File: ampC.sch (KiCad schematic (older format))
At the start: 9 parts, among them U3 MCP6004, U7 Mux

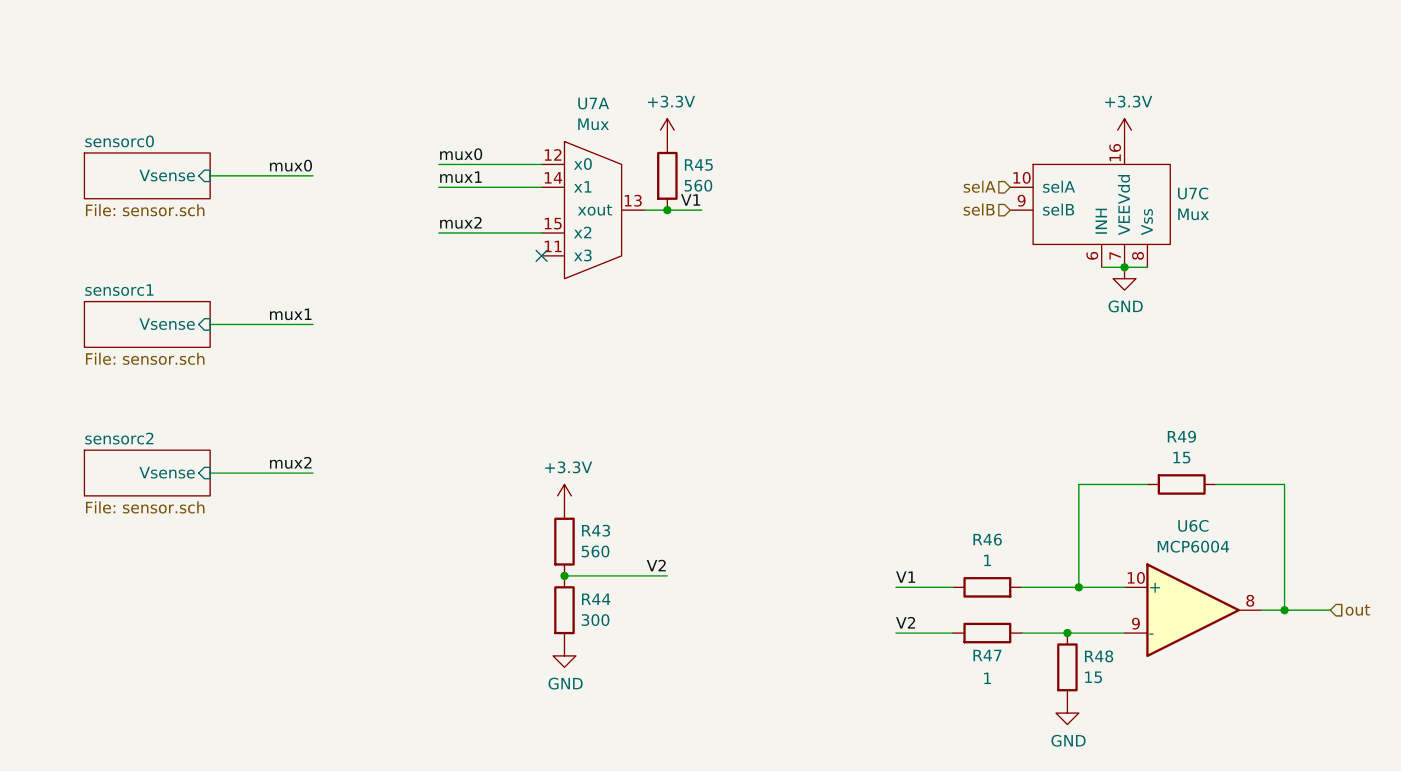
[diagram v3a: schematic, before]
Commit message: fixed drc errors
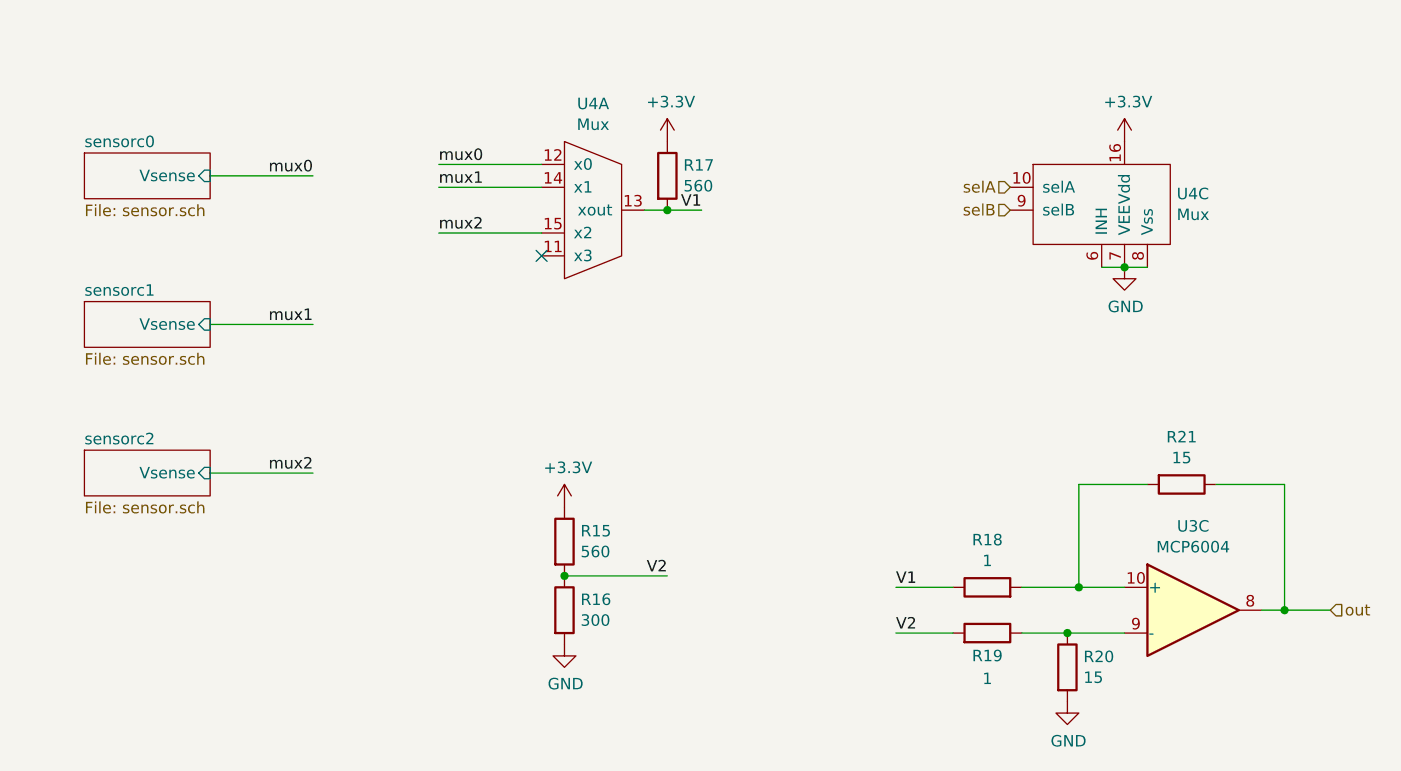
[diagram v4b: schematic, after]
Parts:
- U3: footprint Package_DIP:DIP-14_W7.62mm -> Package_SO:SOIC-16_3.9x9.9mm_P1.27mm
- U7: footprint Package_DIP:DIP-16_W7.62mm -> Package_SO:SOIC-16_3.9x9.9mm_P1.27mm
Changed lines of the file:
@@
 AR Path="/6019C043/60198F28" Ref="R20"  Part="1"
 AR Path="/601B4C16/60198F28" Ref="R48"  Part="1"
-F 0 "R48" H 5520 4096 50  0000 L CNN
+F 0 "R20" H 5520 4096 50  0000 L CNN
 F 1 "15" H 5520 4005 50  0000 L CNN
 F 2 "Resistor_THT:R_Axial_DIN0204_L3.6mm_D1.6mm_P5.08mm_Horizontal" V 5380 4050 50  0001 C CNN
@@
 AR Path="/6019C043/6019D567" Ref="R21"  Part="1"
 AR Path="/601B4C16/6019D567" Ref="R49"  Part="1"
-F 0 "R49" V 5743 3250 50  0000 C CNN
+F 0 "R21" V 5743 3250 50  0000 C CNN
 F 1 "15" V 5834 3250 50  0000 C CNN
 F 2 "Resistor_THT:R_Axial_DIN0204_L3.6mm_D1.6mm_P5.08mm_Horizontal" V 5880 3250 50  0001 C CNN
@@
 AR Path="/6019C043/6019D55D" Ref="R18"  Part="1"
 AR Path="/601B4C16/6019D55D" Ref="R46"  Part="1"
-F 0 "R46" V 5307 3700 50  0000 C CNN
+F 0 "R18" V 5307 3700 50  0000 C CNN
 F 1 "1" V 5216 3700 50  0000 C CNN
 F 2 "Resistor_THT:R_Axial_DIN0204_L3.6mm_D1.6mm_P5.08mm_Horizontal" V 5030 3700 50  0001 C CNN
@@
 AR Path="/6019C043/60198F34" Ref="R19"  Part="1"
 AR Path="/601B4C16/60198F34" Ref="R47"  Part="1"
-F 0 "R47" V 5000 3900 50  0000 C CNN
+F 0 "R19" V 5000 3900 50  0000 C CNN
 F 1 "1" V 4900 3900 50  0000 C CNN
 F 2 "Resistor_THT:R_Axial_DIN0204_L3.6mm_D1.6mm_P5.08mm_Horizontal" V 5030 3900 50  0001 C CNN
@@
 AR Path="/6019C043/6017E433" Ref="R15"  Part="1"
 AR Path="/601B4C16/6017E433" Ref="R43"  Part="1"
-F 0 "R43" H 3320 3546 50  0000 L CNN
+F 0 "R15" H 3320 3546 50  0000 L CNN
 F 1 "560" H 3320 3455 50  0000 L CNN
 F 2 "Resistor_THT:R_Axial_DIN0204_L3.6mm_D1.6mm_P5.08mm_Horizontal" V 3180 3500 50  0001 C CNN
@@
 AR Path="/6019C043/6017E434" Ref="R16"  Part="1"
 AR Path="/601B4C16/6017E434" Ref="R44"  Part="1"
-F 0 "R44" H 3320 3846 50  0000 L CNN
+F 0 "R16" H 3320 3846 50  0000 L CNN
 F 1 "300" H 3320 3755 50  0000 L CNN
 F 2 "Resistor_THT:R_Axial_DIN0204_L3.6mm_D1.6mm_P5.08mm_Horizontal" V 3180 3800 50  0001 C CNN
@@
 AR Path="/601B4C16/601763C1" Ref="U7"  Part="1"
 AR Path="/6019C043/601763C1" Ref="U4"  Part="1"
-F 0 "U7" H 3375 2515 50  0000 C CNN
+F 0 "U4" H 3375 2515 50  0000 C CNN
 F 1 "Mux" H 3375 2424 50  0000 C CNN
-F 2 "Package_DIP:DIP-16_W7.62mm" H 3350 2050 50  0001 C CNN
+F 2 "Package_SO:SOIC-16_3.9x9.9mm_P1.27mm" H 3350 2050 50  0001 C CNN
 F 3 "" H 3350 2050 50  0001 C CNN
 	1    3350 2050
@@
 AR Path="/601B4C16/60176BAF" Ref="U7"  Part="3"
 AR Path="/6019C043/60176BAF" Ref="U4"  Part="3"
-F 0 "U7" H 5928 2221 50  0000 L CNN
+F 0 "U4" H 5928 2221 50  0000 L CNN
 F 1 "Mux" H 5928 2130 50  0000 L CNN
-F 2 "Package_DIP:DIP-16_W7.62mm" H 5700 2100 50  0001 C CNN
+F 2 "Package_SO:SOIC-16_3.9x9.9mm_P1.27mm" H 5700 2100 50  0001 C CNN
 F 3 "" H 5700 2100 50  0001 C CNN
 	3    5700 2100
@@
 AR Path="/6019C043/6018DE62" Ref="U3"  Part="3"
 AR Path="/601B4C16/6018DE62" Ref="U6"  Part="3"
-F 0 "U6" H 6000 4167 50  0000 C CNN
+F 0 "U3" H 6000 4167 50  0000 C CNN
 F 1 "MCP6004" H 6000 4076 50  0000 C CNN
-F 2 "Package_DIP:DIP-14_W7.62mm" H 5950 3900 50  0001 C CNN
+F 2 "Package_SO:SOIC-16_3.9x9.9mm_P1.27mm" H 5950 3900 50  0001 C CNN
 F 3 "http://ww1.microchip.com/downloads/en/DeviceDoc/21733j.pdf" H 6050 4000 50  0001 C CNN
 	3    6000 3800
@@
 AR Path="/6019C043/60205F03" Ref="R17"  Part="1"
 AR Path="/601B4C16/60205F03" Ref="R45"  Part="1"
-F 0 "R45" H 3770 1946 50  0000 L CNN
+F 0 "R17" H 3770 1946 50  0000 L CNN
 F 1 "560" H 3770 1855 50  0000 L CNN
 F 2 "Resistor_THT:R_Axial_DIN0204_L3.6mm_D1.6mm_P5.08mm_Horizontal" V 3630 1900 50  0001 C CNN

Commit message: changed solder pads to be two separate footprints
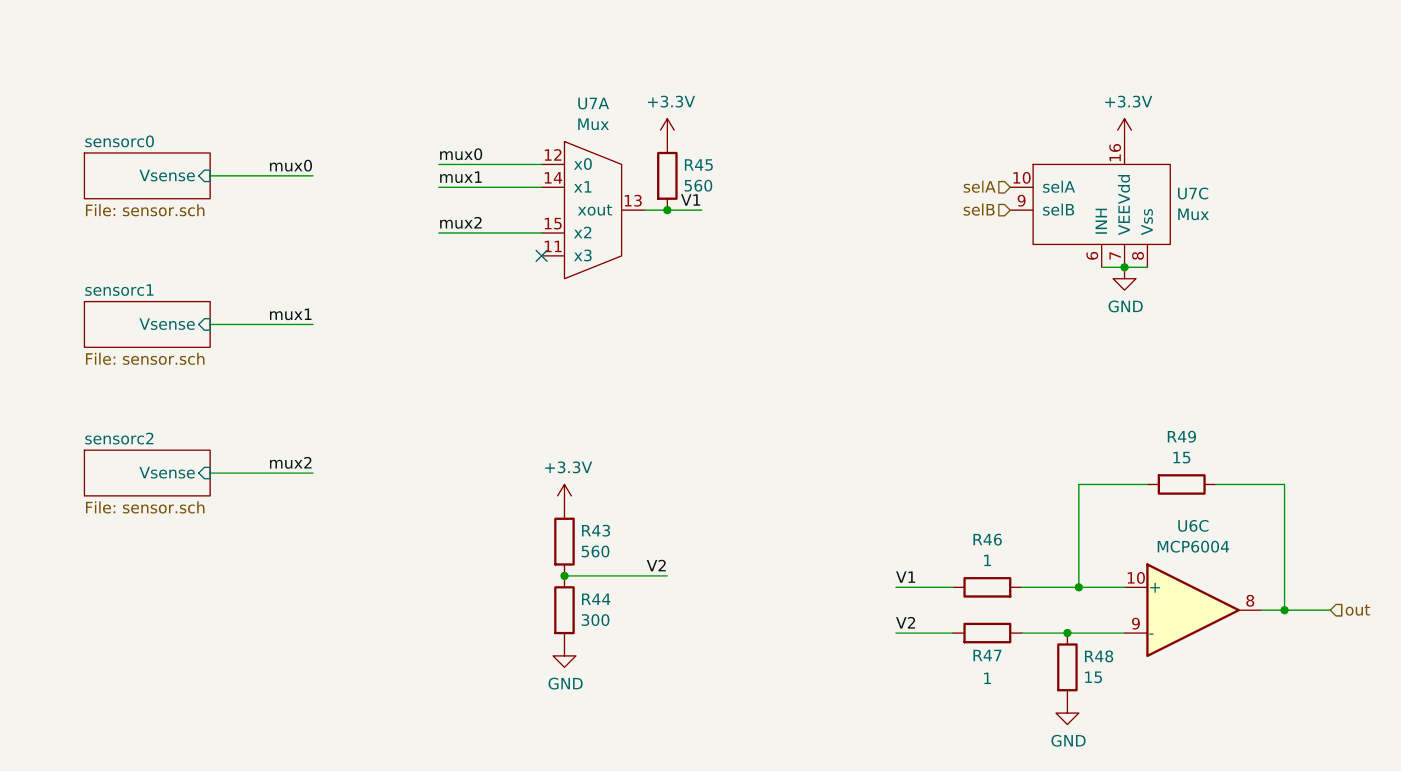
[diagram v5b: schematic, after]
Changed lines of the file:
@@
 AR Path="/6019C043/60198F28" Ref="R20"  Part="1"
 AR Path="/601B4C16/60198F28" Ref="R48"  Part="1"
-F 0 "R20" H 5520 4096 50  0000 L CNN
+F 0 "R48" H 5520 4096 50  0000 L CNN
 F 1 "15" H 5520 4005 50  0000 L CNN
 F 2 "Resistor_THT:R_Axial_DIN0204_L3.6mm_D1.6mm_P5.08mm_Horizontal" V 5380 4050 50  0001 C CNN
@@
 AR Path="/6019C043/6019D567" Ref="R21"  Part="1"
 AR Path="/601B4C16/6019D567" Ref="R49"  Part="1"
-F 0 "R21" V 5743 3250 50  0000 C CNN
+F 0 "R49" V 5743 3250 50  0000 C CNN
 F 1 "15" V 5834 3250 50  0000 C CNN
 F 2 "Resistor_THT:R_Axial_DIN0204_L3.6mm_D1.6mm_P5.08mm_Horizontal" V 5880 3250 50  0001 C CNN
@@
 AR Path="/6019C043/6019D55D" Ref="R18"  Part="1"
 AR Path="/601B4C16/6019D55D" Ref="R46"  Part="1"
-F 0 "R18" V 5307 3700 50  0000 C CNN
+F 0 "R46" V 5307 3700 50  0000 C CNN
 F 1 "1" V 5216 3700 50  0000 C CNN
 F 2 "Resistor_THT:R_Axial_DIN0204_L3.6mm_D1.6mm_P5.08mm_Horizontal" V 5030 3700 50  0001 C CNN
@@
 AR Path="/6019C043/60198F34" Ref="R19"  Part="1"
 AR Path="/601B4C16/60198F34" Ref="R47"  Part="1"
-F 0 "R19" V 5000 3900 50  0000 C CNN
+F 0 "R47" V 5000 3900 50  0000 C CNN
 F 1 "1" V 4900 3900 50  0000 C CNN
 F 2 "Resistor_THT:R_Axial_DIN0204_L3.6mm_D1.6mm_P5.08mm_Horizontal" V 5030 3900 50  0001 C CNN
@@
 AR Path="/6019C043/6017E433" Ref="R15"  Part="1"
 AR Path="/601B4C16/6017E433" Ref="R43"  Part="1"
-F 0 "R15" H 3320 3546 50  0000 L CNN
+F 0 "R43" H 3320 3546 50  0000 L CNN
 F 1 "560" H 3320 3455 50  0000 L CNN
 F 2 "Resistor_THT:R_Axial_DIN0204_L3.6mm_D1.6mm_P5.08mm_Horizontal" V 3180 3500 50  0001 C CNN
@@
 AR Path="/6019C043/6017E434" Ref="R16"  Part="1"
 AR Path="/601B4C16/6017E434" Ref="R44"  Part="1"
-F 0 "R16" H 3320 3846 50  0000 L CNN
+F 0 "R44" H 3320 3846 50  0000 L CNN
 F 1 "300" H 3320 3755 50  0000 L CNN
 F 2 "Resistor_THT:R_Axial_DIN0204_L3.6mm_D1.6mm_P5.08mm_Horizontal" V 3180 3800 50  0001 C CNN
@@
 AR Path="/601B4C16/601763C1" Ref="U7"  Part="1"
 AR Path="/6019C043/601763C1" Ref="U4"  Part="1"
-F 0 "U4" H 3375 2515 50  0000 C CNN
+F 0 "U7" H 3375 2515 50  0000 C CNN
 F 1 "Mux" H 3375 2424 50  0000 C CNN
 F 2 "Package_SO:SOIC-16_3.9x9.9mm_P1.27mm" H 3350 2050 50  0001 C CNN
@@
 AR Path="/601B4C16/60176BAF" Ref="U7"  Part="3"
 AR Path="/6019C043/60176BAF" Ref="U4"  Part="3"
-F 0 "U4" H 5928 2221 50  0000 L CNN
+F 0 "U7" H 5928 2221 50  0000 L CNN
 F 1 "Mux" H 5928 2130 50  0000 L CNN
 F 2 "Package_SO:SOIC-16_3.9x9.9mm_P1.27mm" H 5700 2100 50  0001 C CNN
@@
 AR Path="/6019C043/6018DE62" Ref="U3"  Part="3"
 AR Path="/601B4C16/6018DE62" Ref="U6"  Part="3"
-F 0 "U3" H 6000 4167 50  0000 C CNN
+F 0 "U6" H 6000 4167 50  0000 C CNN
 F 1 "MCP6004" H 6000 4076 50  0000 C CNN
 F 2 "Package_SO:SOIC-16_3.9x9.9mm_P1.27mm" H 5950 3900 50  0001 C CNN
@@
 AR Path="/6019C043/60205F03" Ref="R17"  Part="1"
 AR Path="/601B4C16/60205F03" Ref="R45"  Part="1"
-F 0 "R17" H 3770 1946 50  0000 L CNN
+F 0 "R45" H 3770 1946 50  0000 L CNN
 F 1 "560" H 3770 1855 50  0000 L CNN
 F 2 "Resistor_THT:R_Axial_DIN0204_L3.6mm_D1.6mm_P5.08mm_Horizontal" V 3630 1900 50  0001 C CNN

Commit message: switched over remaining rs to 0805
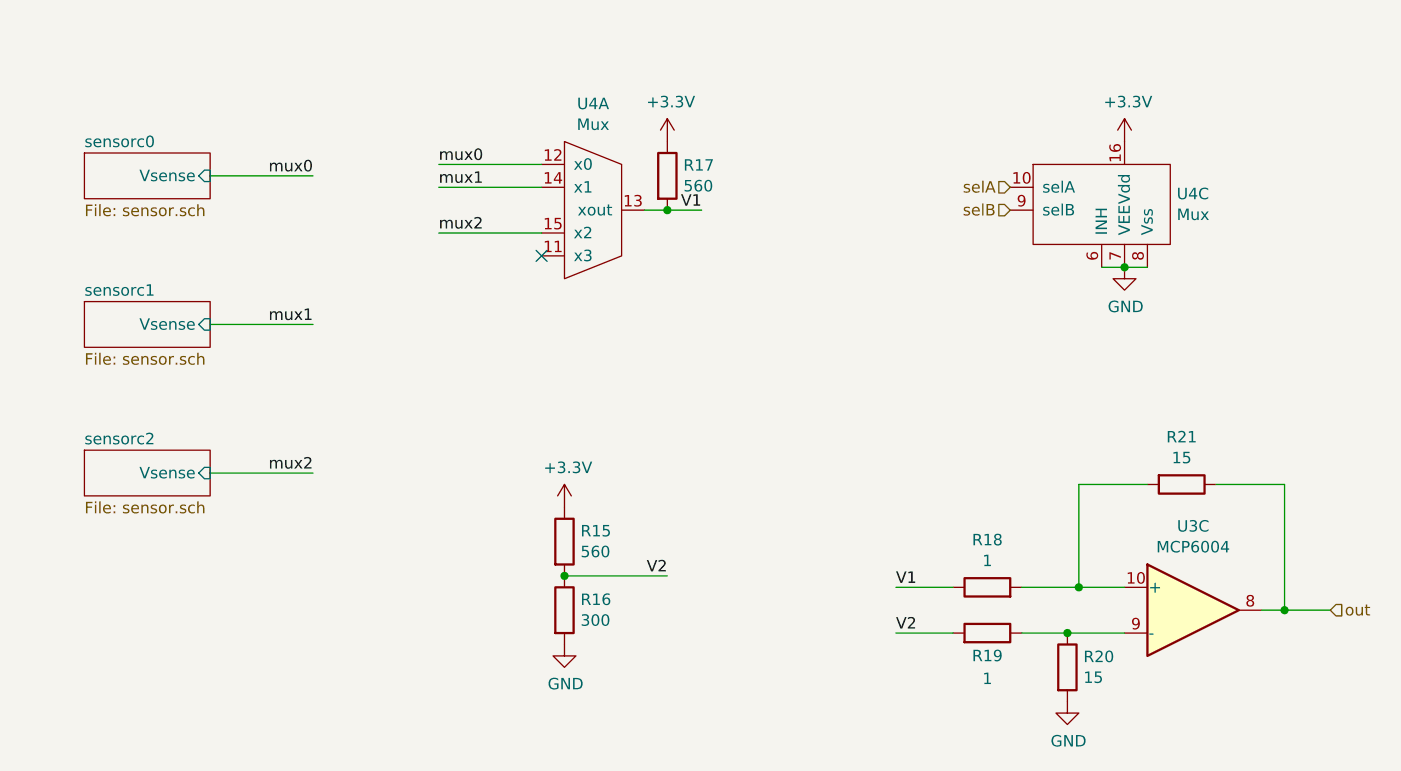
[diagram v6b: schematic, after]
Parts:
- R15, R16, R17, R18, R19, R20, R21: footprint Resistor_THT:R_Axial_DIN0204_L3.6mm_D1.6mm_P5.08mm_Horizontal -> Resistor_SMD:R_0805_2012Metric_Pad1.20x1.40mm_HandSolder
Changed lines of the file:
@@
 AR Path="/6019C043/60198F28" Ref="R20"  Part="1"
 AR Path="/601B4C16/60198F28" Ref="R48"  Part="1"
-F 0 "R48" H 5520 4096 50  0000 L CNN
+F 0 "R20" H 5520 4096 50  0000 L CNN
 F 1 "15" H 5520 4005 50  0000 L CNN
-F 2 "Resistor_THT:R_Axial_DIN0204_L3.6mm_D1.6mm_P5.08mm_Horizontal" V 5380 4050 50  0001 C CNN
+F 2 "Resistor_SMD:R_0805_2012Metric_Pad1.20x1.40mm_HandSolder" V 5380 4050 50  0001 C CNN
 F 3 "~" H 5450 4050 50  0001 C CNN
 	1    5450 4050
@@
 AR Path="/6019C043/6019D567" Ref="R21"  Part="1"
 AR Path="/601B4C16/6019D567" Ref="R49"  Part="1"
-F 0 "R49" V 5743 3250 50  0000 C CNN
+F 0 "R21" V 5743 3250 50  0000 C CNN
 F 1 "15" V 5834 3250 50  0000 C CNN
-F 2 "Resistor_THT:R_Axial_DIN0204_L3.6mm_D1.6mm_P5.08mm_Horizontal" V 5880 3250 50  0001 C CNN
+F 2 "Resistor_SMD:R_0805_2012Metric_Pad1.20x1.40mm_HandSolder" V 5880 3250 50  0001 C CNN
 F 3 "~" H 5950 3250 50  0001 C CNN
 	1    5950 3250
@@
 AR Path="/6019C043/6019D55D" Ref="R18"  Part="1"
 AR Path="/601B4C16/6019D55D" Ref="R46"  Part="1"
-F 0 "R46" V 5307 3700 50  0000 C CNN
+F 0 "R18" V 5307 3700 50  0000 C CNN
 F 1 "1" V 5216 3700 50  0000 C CNN
-F 2 "Resistor_THT:R_Axial_DIN0204_L3.6mm_D1.6mm_P5.08mm_Horizontal" V 5030 3700 50  0001 C CNN
+F 2 "Resistor_SMD:R_0805_2012Metric_Pad1.20x1.40mm_HandSolder" V 5030 3700 50  0001 C CNN
 F 3 "~" H 5100 3700 50  0001 C CNN
 	1    5100 3700
@@
 AR Path="/6019C043/60198F34" Ref="R19"  Part="1"
 AR Path="/601B4C16/60198F34" Ref="R47"  Part="1"
-F 0 "R47" V 5000 3900 50  0000 C CNN
+F 0 "R19" V 5000 3900 50  0000 C CNN
 F 1 "1" V 4900 3900 50  0000 C CNN
-F 2 "Resistor_THT:R_Axial_DIN0204_L3.6mm_D1.6mm_P5.08mm_Horizontal" V 5030 3900 50  0001 C CNN
+F 2 "Resistor_SMD:R_0805_2012Metric_Pad1.20x1.40mm_HandSolder" V 5030 3900 50  0001 C CNN
 F 3 "~" H 5100 3900 50  0001 C CNN
 	1    5100 3900
@@
 AR Path="/6019C043/6017E433" Ref="R15"  Part="1"
 AR Path="/601B4C16/6017E433" Ref="R43"  Part="1"
-F 0 "R43" H 3320 3546 50  0000 L CNN
+F 0 "R15" H 3320 3546 50  0000 L CNN
 F 1 "560" H 3320 3455 50  0000 L CNN
-F 2 "Resistor_THT:R_Axial_DIN0204_L3.6mm_D1.6mm_P5.08mm_Horizontal" V 3180 3500 50  0001 C CNN
+F 2 "Resistor_SMD:R_0805_2012Metric_Pad1.20x1.40mm_HandSolder" V 3180 3500 50  0001 C CNN
 F 3 "~" H 3250 3500 50  0001 C CNN
 	1    3250 3500
@@
 AR Path="/6019C043/6017E434" Ref="R16"  Part="1"
 AR Path="/601B4C16/6017E434" Ref="R44"  Part="1"
-F 0 "R44" H 3320 3846 50  0000 L CNN
+F 0 "R16" H 3320 3846 50  0000 L CNN
 F 1 "300" H 3320 3755 50  0000 L CNN
-F 2 "Resistor_THT:R_Axial_DIN0204_L3.6mm_D1.6mm_P5.08mm_Horizontal" V 3180 3800 50  0001 C CNN
+F 2 "Resistor_SMD:R_0805_2012Metric_Pad1.20x1.40mm_HandSolder" V 3180 3800 50  0001 C CNN
 F 3 "~" H 3250 3800 50  0001 C CNN
 	1    3250 3800
@@
 AR Path="/6019C043/6017E435" Ref="#PWR026"  Part="1"
 AR Path="/601B4C16/6017E435" Ref="#PWR060"  Part="1"
-F 0 "#PWR060" H 3250 3200 50  0001 C CNN
+F 0 "#PWR026" H 3250 3200 50  0001 C CNN
 F 1 "+3.3V" H 3265 3523 50  0000 C CNN
 F 2 "" H 3250 3350 50  0001 C CNN
@@
 AR Path="/6019C043/6019D569" Ref="#PWR027"  Part="1"
 AR Path="/601B4C16/6019D569" Ref="#PWR061"  Part="1"
-F 0 "#PWR061" H 3250 3700 50  0001 C CNN
+F 0 "#PWR027" H 3250 3700 50  0001 C CNN
 F 1 "GND" H 3255 3777 50  0000 C CNN
 F 2 "" H 3250 3950 50  0001 C CNN
@@
 AR Path="/6019C043/6019D555" Ref="#PWR029"  Part="1"
 AR Path="/601B4C16/6019D555" Ref="#PWR063"  Part="1"
-F 0 "#PWR063" H 5450 3950 50  0001 C CNN
+F 0 "#PWR029" H 5450 3950 50  0001 C CNN
 F 1 "GND" H 5455 4027 50  0000 C CNN
 F 2 "" H 5450 4200 50  0001 C CNN
@@
 AR Path="/6019C043/6019D563" Ref="#PWR031"  Part="1"
 AR Path="/601B4C16/6019D563" Ref="#PWR065"  Part="1"
-F 0 "#PWR065" H 5700 2050 50  0001 C CNN
+F 0 "#PWR031" H 5700 2050 50  0001 C CNN
 F 1 "GND" H 5705 2127 50  0000 C CNN
 F 2 "" H 5700 2300 50  0001 C CNN
@@
 AR Path="/6019C043/6019D564" Ref="#PWR030"  Part="1"
 AR Path="/601B4C16/6019D564" Ref="#PWR064"  Part="1"
-F 0 "#PWR064" H 5700 1600 50  0001 C CNN
+F 0 "#PWR030" H 5700 1600 50  0001 C CNN
 F 1 "+3.3V" H 5715 1923 50  0000 C CNN
 F 2 "" H 5700 1750 50  0001 C CNN
@@
 AR Path="/601B4C16/601763C1" Ref="U7"  Part="1"
 AR Path="/6019C043/601763C1" Ref="U4"  Part="1"
-F 0 "U7" H 3375 2515 50  0000 C CNN
+F 0 "U4" H 3375 2515 50  0000 C CNN
 F 1 "Mux" H 3375 2424 50  0000 C CNN
 F 2 "Package_SO:SOIC-16_3.9x9.9mm_P1.27mm" H 3350 2050 50  0001 C CNN
@@
 AR Path="/601B4C16/60176BAF" Ref="U7"  Part="3"
 AR Path="/6019C043/60176BAF" Ref="U4"  Part="3"
-F 0 "U7" H 5928 2221 50  0000 L CNN
+F 0 "U4" H 5928 2221 50  0000 L CNN
 F 1 "Mux" H 5928 2130 50  0000 L CNN
 F 2 "Package_SO:SOIC-16_3.9x9.9mm_P1.27mm" H 5700 2100 50  0001 C CNN
@@
 AR Path="/6019C043/6018DE62" Ref="U3"  Part="3"
 AR Path="/601B4C16/6018DE62" Ref="U6"  Part="3"
-F 0 "U6" H 6000 4167 50  0000 C CNN
+F 0 "U3" H 6000 4167 50  0000 C CNN
 F 1 "MCP6004" H 6000 4076 50  0000 C CNN
 F 2 "Package_SO:SOIC-16_3.9x9.9mm_P1.27mm" H 5950 3900 50  0001 C CNN
@@
 AR Path="/6019C043/60205F03" Ref="R17"  Part="1"
 AR Path="/601B4C16/60205F03" Ref="R45"  Part="1"
-F 0 "R45" H 3770 1946 50  0000 L CNN
+F 0 "R17" H 3770 1946 50  0000 L CNN
 F 1 "560" H 3770 1855 50  0000 L CNN
-F 2 "Resistor_THT:R_Axial_DIN0204_L3.6mm_D1.6mm_P5.08mm_Horizontal" V 3630 1900 50  0001 C CNN
+F 2 "Resistor_SMD:R_0805_2012Metric_Pad1.20x1.40mm_HandSolder" V 3630 1900 50  0001 C CNN
 F 3 "~" H 3700 1900 50  0001 C CNN
 	1    3700 1900
@@
 AR Path="/6019C043/60206022" Ref="#PWR028"  Part="1"
 AR Path="/601B4C16/60206022" Ref="#PWR062"  Part="1"
-F 0 "#PWR062" H 3700 1600 50  0001 C CNN
+F 0 "#PWR028" H 3700 1600 50  0001 C CNN
 F 1 "+3.3V" H 3715 1923 50  0000 C CNN
 F 2 "" H 3700 1750 50  0001 C CNN

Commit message: fixed issue with wrong amp footprint
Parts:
- U3: footprint Package_SO:SOIC-16_3.9x9.9mm_P1.27mm -> Package_SO:SOIC-14_3.9x8.7mm_P1.27mm
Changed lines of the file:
@@
 F 0 "U3" H 6000 4167 50  0000 C CNN
 F 1 "MCP6004" H 6000 4076 50  0000 C CNN
-F 2 "Package_SO:SOIC-16_3.9x9.9mm_P1.27mm" H 5950 3900 50  0001 C CNN
+F 2 "Package_SO:SOIC-14_3.9x8.7mm_P1.27mm" H 5950 3900 50  0001 C CNN
 F 3 "http://ww1.microchip.com/downloads/en/DeviceDoc/21733j.pdf" H 6050 4000 50  0001 C CNN
 	3    6000 3800
